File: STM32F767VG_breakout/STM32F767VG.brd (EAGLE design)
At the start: 89.8 x 35.5 mm, 43 parts, among them IC1 STM32F767VGT6, IC2 L7805CV, IC3 LD117AS33TR, X4 8MHz, X5 32.768kHz

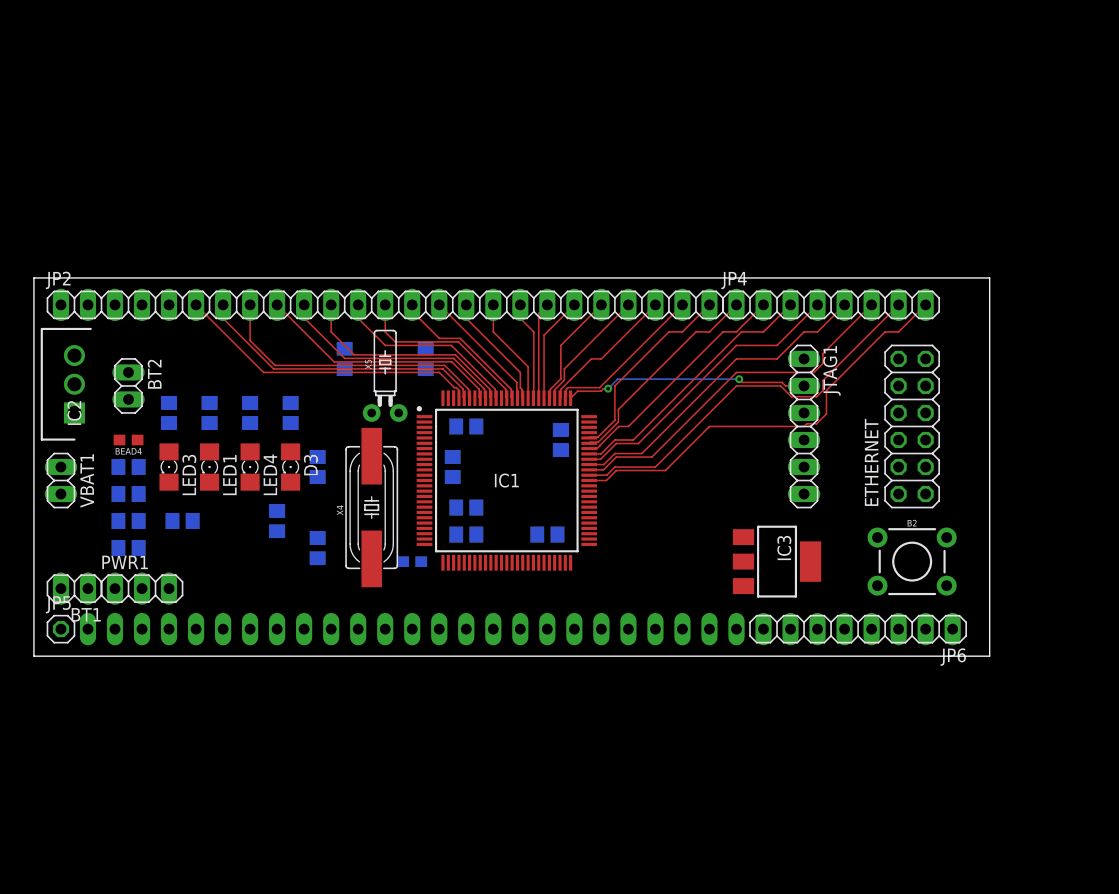
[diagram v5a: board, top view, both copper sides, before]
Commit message: Replacement
Rotated the microcontroller. Will route the side pins later.
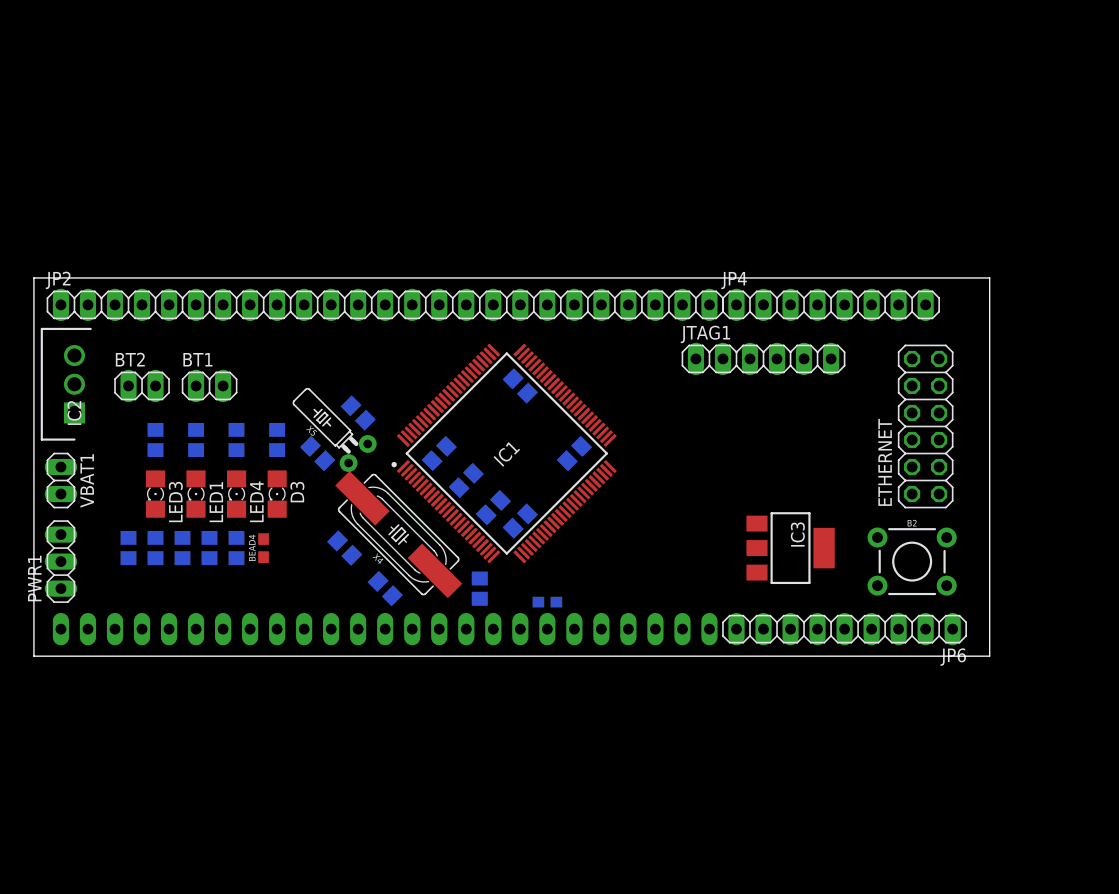
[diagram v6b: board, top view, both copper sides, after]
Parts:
- removed JP5: (no value), pinhead:1X01
- JP6: device pinhead:1X08 -> pinhead:1X09
- moved BT1 22.9 mm to (16.5, 45.7), turned to 0 degrees
- moved R1 20.1 mm to (41.9, 26.7)
- moved BEAD4 16.3 mm to (21.6, 30.5), turned to 90 degrees
- moved BEAD3 13.3 mm to (48.3, 25.4)
- moved C5 12.7 mm to (19.1, 30.5), turned to 270 degrees
- moved C9 9.25 mm to (26.7, 39.4), turned to 225 degrees
- moved C10 9.16 mm to (16.5, 30.5), turned to 90 degrees
- moved C8 8.13 mm to (30.5, 43.2), turned to 225 degrees
- moved C7 8.03 mm to (29.2, 30.5), turned to 45 degrees
- moved PWR1 8.03 mm to (2.54, 29.2), turned to 90 degrees
- moved JTAG1 7.41 mm to (68.6, 48.3), turned to 0 degrees
- moved C6 7.41 mm to (33.0, 26.7), turned to 225 degrees
- moved C1 6.35 mm to (45.7, 45.7), turned to 225 degrees
- moved C16 5.68 mm to (8.89, 30.5), turned to 270 degrees
- moved R2 5.68 mm to (14.0, 30.5), turned to 90 degrees
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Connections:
- removed net N$1: IC1.46, JP1.3
- removed net N$10: IC1.37, JP1.12
- removed net N$11: IC1.36, JP1.13
- removed net N$12: IC1.35, JP1.14
- removed net N$18: IC1.34, JP1.15
- removed net N$2: IC1.45, JP1.4
- removed net N$20: IC1.30, JP1.16
- removed net N$24: IC1.29, JP1.17
- removed net N$25: IC1.28, JP1.18
- removed net N$3: IC1.44, JP1.5
- removed net N$33: IC1.92, JP2.10
- removed net N$34: IC1.93, JP2.9
- removed net N$35: IC1.95, JP2.8
- removed net N$36: IC1.96, JP2.7
- removed net N$37: IC1.97, JP2.6
- removed net N$4: IC1.43, JP1.6
- removed net N$43: IC1.84, JP2.17
- removed net N$45: IC1.82, JP2.19
- removed net N$48: IC1.79, JP2.22
- removed net N$49: IC1.78, JP2.23
- removed net N$5: IC1.42, JP1.7
- removed net N$50: IC1.77, JP2.24
- removed net N$58: IC1.87, JP2.14
- removed net N$59: IC1.86, JP2.15
- removed net N$6: IC1.41, JP1.8
- removed net N$60: IC1.85, JP2.16
- removed net N$64: IC1.80, JP2.21
- removed net N$65: IC1.81, JP2.20
- removed net N$67: IC1.83, JP2.18
- removed net N$7: IC1.40, JP1.9
- removed net N$71: IC1.91, JP2.11
- removed net N$72: IC1.90, JP2.12
- removed net N$8: IC1.39, JP1.10
- removed net N$9: IC1.38, JP1.11
- new net PA15: IC1.77
- new net PA4: IC1.28
- new net PA5: IC1.29
- new net PA6: IC1.30
- new net PB0: IC1.34
- new net PB1: IC1.35
- new net PB10: IC1.46
- new net PB2: IC1.36
- new net PB4: IC1.90
- new net PB5: IC1.91
- new net PB6: IC1.92
- new net PB7: IC1.93
- new net PB8: IC1.95
- new net PB9: IC1.96
- new net PC10: IC1.78
- new net PC11: IC1.79
- new net PC12: IC1.80
- new net PD0: IC1.81
- new net PD1: IC1.82
- new net PD2: IC1.83
- new net PD3: IC1.84
- new net PD4: IC1.85
- new net PD5: IC1.86
- new net PD6: IC1.87
- new net PE0: IC1.97
- new net PE1: IC1.98
- new net PE10: IC1.40
- new net PE11: IC1.41
- new net PE12: IC1.42
- new net PE13: IC1.43
- new net PE14: IC1.44
- new net PE15: IC1.45
- new net PE7: IC1.37
- new net PE8: IC1.38
- new net PE9: IC1.39
- net 12V: now also JP1.25; no longer JP5.1
- net PA0: no longer JP1.20
- net PA10: no longer JP4.2
- net PA11: no longer JP4.1
- net PA12: no longer JP2.25
- net PA3: no longer JP1.19
- net PA8: no longer JP4.4
- net PA9: no longer JP4.3
- net PB14: no longer JP1.2
- net PB15: no longer JP1.1
- net PC0: no longer JP1.23
- net PC13: no longer JP1.24
- net PC2: no longer JP1.22
- net PC3: no longer JP1.21
- net PC6: no longer JP4.8
- net PC7: no longer JP4.7
- net PC8: no longer JP4.6
- net PC9: no longer JP4.5
- net PD10: no longer JP6.6
- net PD11: no longer JP6.5
- net PD12: no longer JP6.4
- net PD13: no longer JP6.3
- net PD14: no longer JP6.2
- net PD15: no longer JP6.1
- net PD7: no longer JP2.13
- net PD8: no longer JP6.8
- net PD9: no longer JP6.7
- net PE2: no longer IC1.98, JP2.4, JP2.5
- net PE3: no longer JP2.3
- net PE4: no longer JP2.2
- net PE5: no longer JP2.1
- net PE6: no longer JP1.25
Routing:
- net PC6: track 39.8 -> 0.00 mm
- net PC7: track 37.1 -> 0.00 mm
- net PC8: track 33.5 -> 0.00 mm
- net PC9: track 30.2 -> 0.00 mm
- net N$37: track 28.8 -> 0.00 mm
- net N$36: track 27.5 -> 0.00 mm
- net PA8: track 27.5 -> 0.00 mm
- net N$35: track 26.7 -> 0.00 mm
- net PA9: track 24.7 -> 0.00 mm
- net N$34: track 23.2 -> 0.00 mm
- net TCK: track 22.9 -> 0.00 mm, vias 2 -> 0
- net PA10: track 22.0 -> 0.00 mm
- net N$33: track 21.8 -> 0.00 mm
- net N$71: track 20.6 -> 0.00 mm
- net PA11: track 19.9 -> 0.00 mm
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
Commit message: Ethernet and Crystal Rounting
First draft of ethernet and crystal routing. If ok, then will move on to sid epin headers
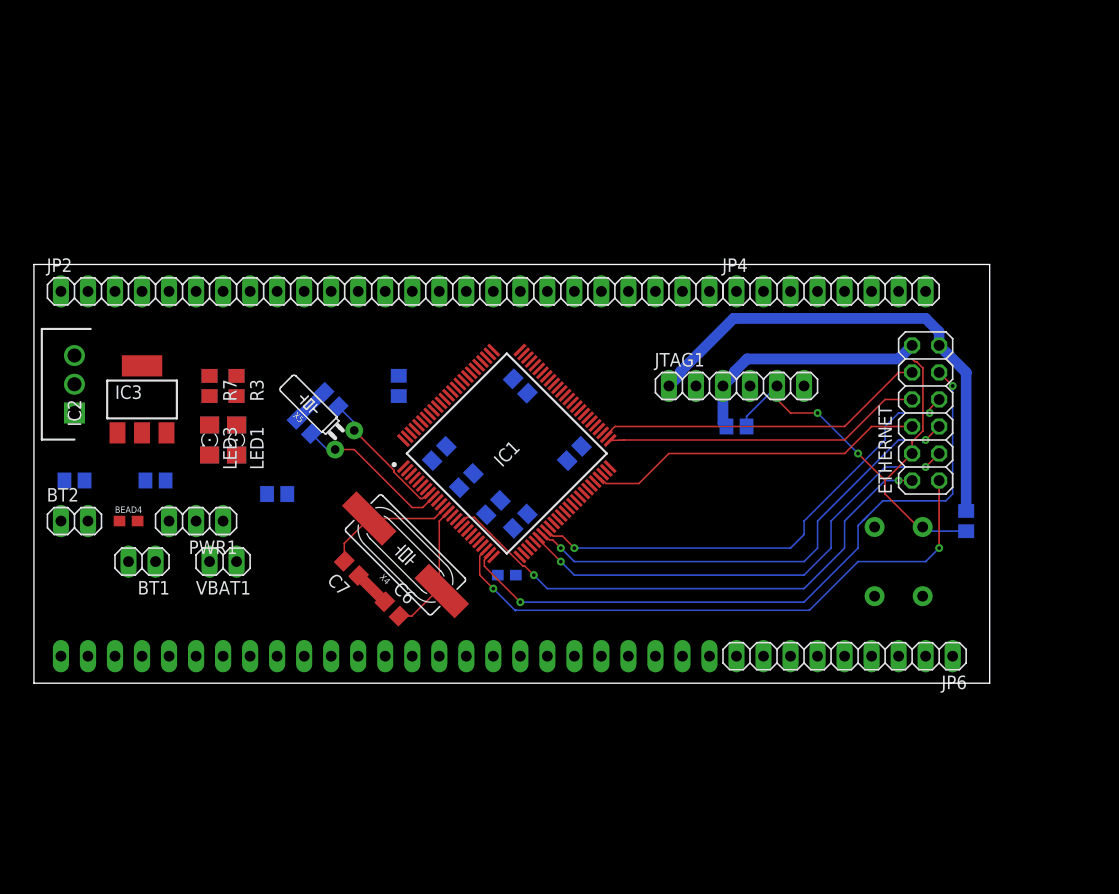
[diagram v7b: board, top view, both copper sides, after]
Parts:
- moved IC3 62.5 mm to (10.2, 44.5), turned to 0 degrees
- moved C10 50.8 mm to (66.0, 41.9), turned to 0 degrees
- moved R1 46.2 mm to (87.6, 33.0), turned to 270 degrees
- moved R2 25.4 mm to (34.3, 45.7)
- moved BT1 17.7 mm to (10.2, 29.2), turned to 180 degrees
- moved VBAT1 17.0 mm to (17.8, 29.2), turned to 180 degrees
- moved BT2 14.2 mm to (3.81, 33.0)
- moved PWR1 13.3 mm to (15.2, 33.0), turned to 180 degrees
- moved BEAD4 13.0 mm to (8.89, 33.0), turned to 0 degrees
- moved C16 8.13 mm to (3.81, 36.8), turned to 0 degrees
- moved LED3 7.18 mm to (16.5, 40.6)
- moved R7 7.18 mm to (16.5, 45.7), flipped to the top
- moved C5 6.35 mm to (22.9, 35.6), turned to 180 degrees
- moved LED1 6.35 mm to (19.1, 40.6)
- moved R3 6.35 mm to (19.1, 45.7), flipped to the top
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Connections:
- new net N$1: JP1.24
- new net N$10: JP1.15
- new net N$11: JP1.14
- new net N$12: JP1.13
- new net N$16: JP1.12
- new net N$18: JP1.11
- new net N$19: JP1.10
- new net N$2: JP1.23
- new net N$20: JP1.9
- new net N$24: JP1.8
- new net N$25: JP1.7
- new net N$28: JP1.6
- new net N$29: JP1.5
- new net N$3: JP1.22
- new net N$30: JP1.4
- new net N$31: JP1.3
- new net N$32: JP1.2
- new net N$33: JP1.1
- new net N$34: JP6.9
- new net N$35: JP6.8
- new net N$36: JP6.7
- new net N$37: JP6.6
- new net N$38: JP6.5
- new net N$39: JP6.4
- new net N$4: JP1.21
- new net N$40: JP6.3
- new net N$41: JP6.2
- new net N$42: JP6.1
- new net N$43: JP2.1
- new net N$44: JP2.2
- new net N$45: JP2.3
- new net N$46: JP2.4
- new net N$47: JP2.5
- new net N$48: JP2.6
- new net N$49: JP2.7
- new net N$5: JP1.20
- new net N$50: JP2.8
- new net N$51: JP2.9
- new net N$52: JP2.10
- new net N$53: JP2.11
- new net N$54: JP2.12
- new net N$55: JP2.13
- new net N$56: JP2.14
- new net N$57: JP2.15
- new net N$58: JP2.16
- new net N$59: JP2.17
- new net N$6: JP1.19
- new net N$60: JP2.18
- new net N$61: JP2.19
- new net N$62: JP2.20
- new net N$63: JP2.21
- new net N$64: JP2.22
- new net N$65: JP2.24
- new net N$66: JP2.23
- new net N$67: JP2.25
- new net N$68: JP4.4
- new net N$69: JP4.5
- new net N$7: JP1.18
- new net N$70: JP4.6
- new net N$71: JP4.7
- new net N$72: JP4.8
- new net N$73: JP4.3
- new net N$74: JP4.2
- new net N$75: JP4.1
- new net N$8: JP1.17
- new net N$9: JP1.16
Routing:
- net MDIO: track 0.00 -> 64.9 mm, vias 0 -> 2
- net NINT: track 0.00 -> 56.0 mm, vias 0 -> 2
- net MDC: track 0.00 -> 51.2 mm, vias 0 -> 2
- net VDD: track 0.00 -> 46.6 mm
- net RXD0: track 0.00 -> 45.5 mm, vias 0 -> 2
- net CRS_DV: track 0.00 -> 45.4 mm, vias 0 -> 2
- net RXD1: track 0.00 -> 45.1 mm, vias 0 -> 2
- net NRST: track 0.00 -> 43.3 mm, vias 0 -> 2
- net TXEN: track 0.00 -> 31.9 mm
- net TXD1: track 0.00 -> 31.3 mm
- net GND: track 0.00 -> 30.5 mm
- net TXD0: track 0.00 -> 30.0 mm
- net N$15: track 0.00 -> 14.8 mm
- net N$14: track 0.00 -> 12.9 mm
- net N$21: track 0.00 -> 12.8 mm
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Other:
- board size 89.8 x 35.5 mm -> 89.8 x 39.4 mm

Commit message: First try at routing everything
Currently it's a mess, so will redo most of the routing. But this is the current progress
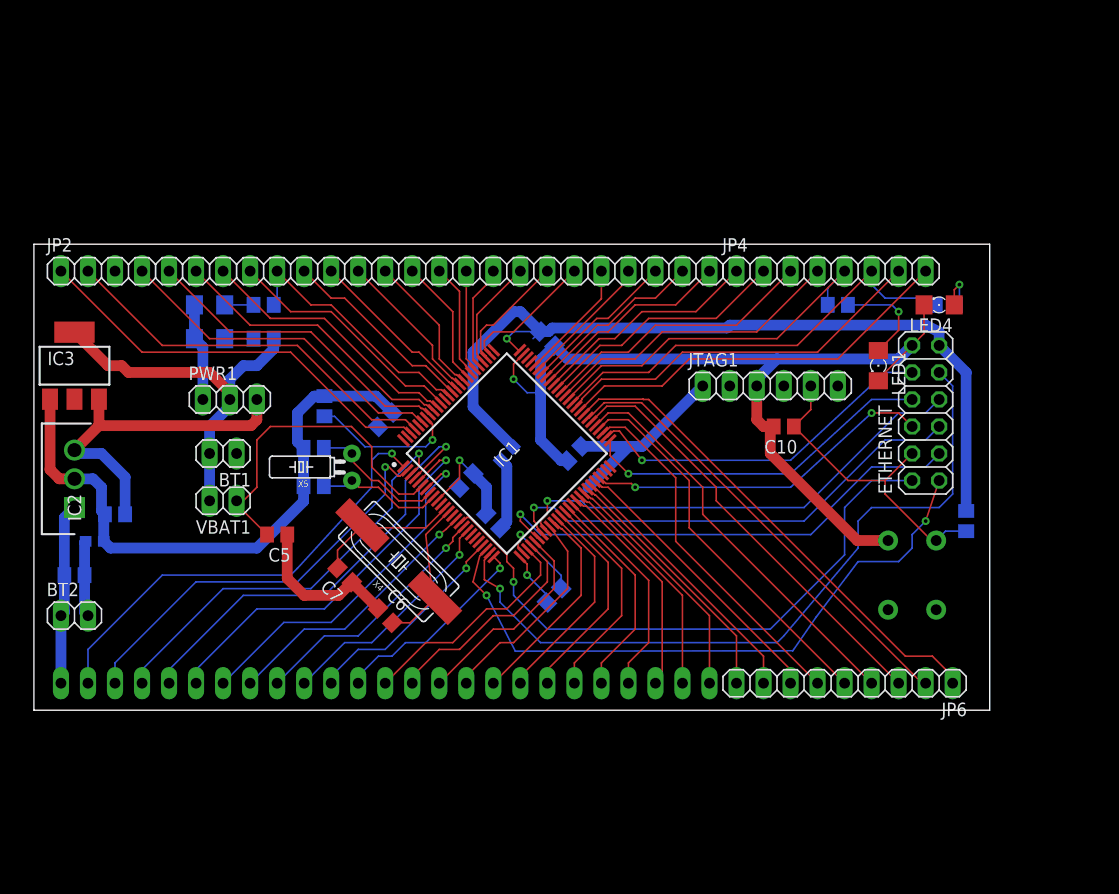
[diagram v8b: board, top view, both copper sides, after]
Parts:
- moved LED4 69.7 mm to (85.1, 53.3), flipped to the top, turned to 180 degrees
- moved R8 69.6 mm to (85.7, 53.3), turned to 180 degrees
- moved LED1 60.7 mm to (79.4, 47.6)
- moved R3 57.0 mm to (75.6, 53.3), flipped to the bottom, turned to 180 degrees
- moved LED3 12.7 mm to (16.5, 53.3), flipped to the bottom, turned to 0 degrees
- moved BT1 12.7 mm to (17.8, 39.4)
- moved PWR1 11.9 mm to (18.4, 44.5), turned to 0 degrees
- moved BEAD3 11.4 mm to (44.5, 39.4), turned to 315 degrees
- moved D3 9.86 mm to (16.5, 50.2), turned to 0 degrees
- moved R7 9.16 mm to (21.6, 53.3), flipped to the bottom, turned to 0 degrees
- moved BT2 8.89 mm to (3.81, 24.1)
- moved IC2 8.89 mm to (3.81, 34.3)
- moved C16 8.89 mm to (3.81, 27.9)
- moved C13 7.67 mm to (48.9, 26.0), turned to 315 degrees
- moved R2 7.24 mm to (27.3, 43.8)
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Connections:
- removed net N$1: JP1.24
- removed net N$10: JP1.15
- removed net N$11: JP1.14
- removed net N$12: JP1.13
- removed net N$16: JP1.12
- removed net N$18: JP1.11
- removed net N$19: JP1.10
- removed net N$2: JP1.23
- removed net N$20: JP1.9
- removed net N$24: JP1.8
- removed net N$25: JP1.7
- removed net N$28: JP1.6
- removed net N$29: JP1.5
- removed net N$3: JP1.22
- removed net N$30: JP1.4
- removed net N$31: JP1.3
- removed net N$32: JP1.2
- removed net N$33: JP1.1
- removed net N$34: JP6.9
- removed net N$35: JP6.8
- removed net N$36: JP6.7
- removed net N$37: JP6.6
- removed net N$38: JP6.5
- removed net N$39: JP6.4
- removed net N$4: JP1.21
- removed net N$40: JP6.3
- removed net N$41: JP6.2
- removed net N$42: JP6.1
- removed net N$43: JP2.1
- removed net N$44: JP2.2
- removed net N$45: JP2.3
- removed net N$46: JP2.4
- removed net N$47: JP2.5
- removed net N$48: JP2.6
- removed net N$49: JP2.7
- removed net N$5: JP1.20
- removed net N$50: JP2.8
- removed net N$51: JP2.9
- removed net N$52: JP2.10
- removed net N$53: JP2.11
- removed net N$54: JP2.12
- removed net N$55: JP2.13
- removed net N$56: JP2.14
- removed net N$57: JP2.15
- removed net N$58: JP2.16
- removed net N$59: JP2.17
- removed net N$6: JP1.19
- removed net N$60: JP2.18
- removed net N$61: JP2.19
- removed net N$62: JP2.20
- removed net N$63: JP2.21
- removed net N$64: JP2.22
- removed net N$65: JP2.24
- removed net N$66: JP2.23
- removed net N$67: JP2.25
- removed net N$68: JP4.4
- removed net N$69: JP4.5
- removed net N$7: JP1.18
- removed net N$70: JP4.6
- removed net N$71: JP4.7
- removed net N$72: JP4.8
- removed net N$73: JP4.3
- removed net N$74: JP4.2
- removed net N$75: JP4.1
- removed net N$8: JP1.17
- removed net N$9: JP1.16
- net PA0: now also JP1.15
- net PA10: now also JP2.23
- net PA11: now also JP2.22
- net PA12: now also JP2.21
- net PA15: now also JP2.20
- net PA3: now also JP1.14
- net PA4: now also JP1.13
- net PA5: now also JP1.12
- net PA6: now also JP1.11
- net PA8: now also JP2.25
- net PA9: now also JP2.24
- net PB0: now also JP1.10
- net PB1: now also JP1.9
- net PB10: now also JP6.7
- net PB14: now also JP6.6
- net PB15: now also JP6.5
- net PB2: now also JP1.8
- net PB4: now also JP2.8
- net PB5: now also JP2.7
- net PB6: now also JP2.6
- net PB7: now also JP2.5
- net PB8: now also JP2.4
- net PB9: now also JP2.3
- net PC0: now also JP1.18
- net PC10: now also JP2.19
- net PC11: now also JP2.18
- net PC12: now also JP2.17
- net PC13: now also JP1.19
- net PC2: now also JP1.17
- net PC3: now also JP1.16
- net PC6: now also JP4.4
- net PC7: now also JP4.3
- net PC8: now also JP4.2
- net PC9: now also JP4.1
- net PD0: now also JP2.16
- net PD1: now also JP2.15
- net PD10: now also JP6.2
- net PD11: now also JP6.1
- net PD12: now also JP4.8
- net PD13: now also JP4.7
- net PD14: now also JP4.6
- net PD15: now also JP4.5
- net PD2: now also JP2.14
- net PD3: now also JP2.13
- net PD4: now also JP2.12
- net PD5: now also JP2.11
- net PD6: now also JP2.10
- net PD7: now also JP2.9
- net PD8: now also JP6.4
- net PD9: now also JP6.3
- net PE0: now also JP2.2
- net PE1: now also JP2.1
- net PE10: now also JP1.4
- net PE11: now also JP1.3
- net PE12: now also JP1.2
- net PE13: now also JP1.1
- net PE14: now also JP6.9
- net PE15: now also JP6.8
- net PE2: now also JP1.24
- net PE3: now also JP1.23
- net PE4: now also JP1.22
- net PE5: now also JP1.21
- net PE6: now also JP1.20
- net PE7: now also JP1.7
- net PE8: now also JP1.6
- net PE9: now also JP1.5
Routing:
- net GND: track 30.5 -> 185.1 mm, vias 0 -> 3
- net VDD: track 46.6 -> 144.9 mm, vias 0 -> 2
- net PD11: track 0.00 -> 46.7 mm
- net PD10: track 0.00 -> 43.3 mm
- net PE2: track 0.00 -> 42.7 mm, vias 0 -> 1
- net PE5: track 0.00 -> 42.0 mm, vias 0 -> 1
- net PD14: track 0.00 -> 41.3 mm
- net PD9: track 0.00 -> 41.0 mm
- net PE4: track 0.00 -> 39.5 mm, vias 0 -> 1
- net PE1: track 0.00 -> 39.2 mm
- net PE3: track 0.00 -> 39.1 mm, vias 0 -> 1
- net PD8: track 0.00 -> 38.5 mm
- net PD12: track 0.00 -> 37.9 mm
- net PE6: track 0.00 -> 37.9 mm, vias 0 -> 1
- net PE0: track 0.00 -> 36.9 mm
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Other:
- board size 89.8 x 39.4 mm -> 89.8 x 43.8 mm
